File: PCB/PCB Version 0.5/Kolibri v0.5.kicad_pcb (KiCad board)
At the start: 8 copper layers, 38 x 38 mm, 212 parts, among them IC1 SX1280IMLTRT, IC2 RFX2401C, IC3 SX1280IMLTRT, IC4 RFX2401C, IC5 LMR38025SDRRR, IC6 LMR38025SDRRR, J1 USB_C_Receptacle_USB2.0_16P, J2 Conn_01x04_MountingPin, J3 Conn_Coaxial_Small, J4 Conn_Coaxial_Small, J5 Conn_01x08_MountingPin, J6 Conn_01x06_MountingPin, J7 Conn_01x06_MountingPin, J8 Conn_01x03_MountingPin, J9 Micro_SD_Card_Det1, Q1 BSS138, U1 RP2350A, U10 W25Q16JVUXIQ, U2 BMI270, U3 ESP32-U4WDH, U4 TPS2116DRL, U5 AT7456E, U6 LP5912-3.3DRV, U7 TPS746-3.3DRV, U8 WE-TVS-824015043, U9 TLV9002S_RUG_X2QFN, Y1 Crystal_GND24, Y2 Crystal_GND24, Y3 Crystal_GND24, Y4 Crystal_GND24, Y5 Crystal_GND24

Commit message: wip backup
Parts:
- removed S1: Goertek SPL06-001, Kolibri custom:Goertek SPL06-001
- added U11: LPS22HB, Package_LGA:ST_HLGA-10_2x2mm_P0.5mm_LayoutBorder3x2y, F.Cu at (124.0, 107.0)
- C25, C26, C27, C28, C29, C30, C31, C33, C34, C35, C36, C37, C38, C39, C40, C49, C50, C53, C54: footprint Capacitor_SMD:C_0402_1005Metric -> Capacitor_SMD:C_0402_1005Metric_Pad0.74x0.62mm_HandSolder
- C66, C72, D14, D15, D16, D17, D18, J7, P10, P11: moved to B.Cu
- C67, C70, C77, C78: footprint Capacitor_SMD:C_0402_1005Metric -> Capacitor_SMD:C_0402_1005Metric_Pad0.74x0.62mm_HandSolder; moved to B.Cu
- J8: moved to F.Cu
- L2: footprint Inductor_SMD:L_0402_1005Metric -> Inductor_SMD:L_0402_1005Metric_Pad0.77x0.64mm_HandSolder
- R10, R11, R12, R9: footprint Resistor_SMD:R_0402_1005Metric -> Resistor_SMD:R_0402_1005Metric_Pad0.72x0.64mm_HandSolder
- R15, R16, R19, R20, R25, R28, R29, R30, R31, R32: footprint Resistor_SMD:R_0402_1005Metric -> Resistor_SMD:R_0402_1005Metric_Pad0.72x0.64mm_HandSolder; moved to B.Cu
- moved C16 89.5 mm to (106.9, 78.8)
- moved D1 83.5 mm to (106.8, 77.2)
- moved J7 83.4 mm to (92.3, 85.0)
- moved J6 80.4 mm to (95.2, 85.0), turned to 180 degrees
- moved R5 73.3 mm to (88.8, 114.8), turned to -90 degrees
- moved C23 67.4 mm to (127.4, 105.6)
- moved C24 67.4 mm to (127.4, 107.6)
- moved R6 60.8 mm to (101.4, 116.6), turned to -90 degrees
- moved P18 58.3 mm to (114.5, 108.5)
- moved P28 57.8 mm to (117.0, 106.0)
- moved P23 55.8 mm to (114.5, 103.5)
- moved P19 54.4 mm to (114.5, 106.0)
- moved P29 48.2 mm to (118.0, 68.2)
- moved P34 48.2 mm to (115.3, 72.7)
- moved C78 39.5 mm to (110.0, 104.0), turned to 180 degrees
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
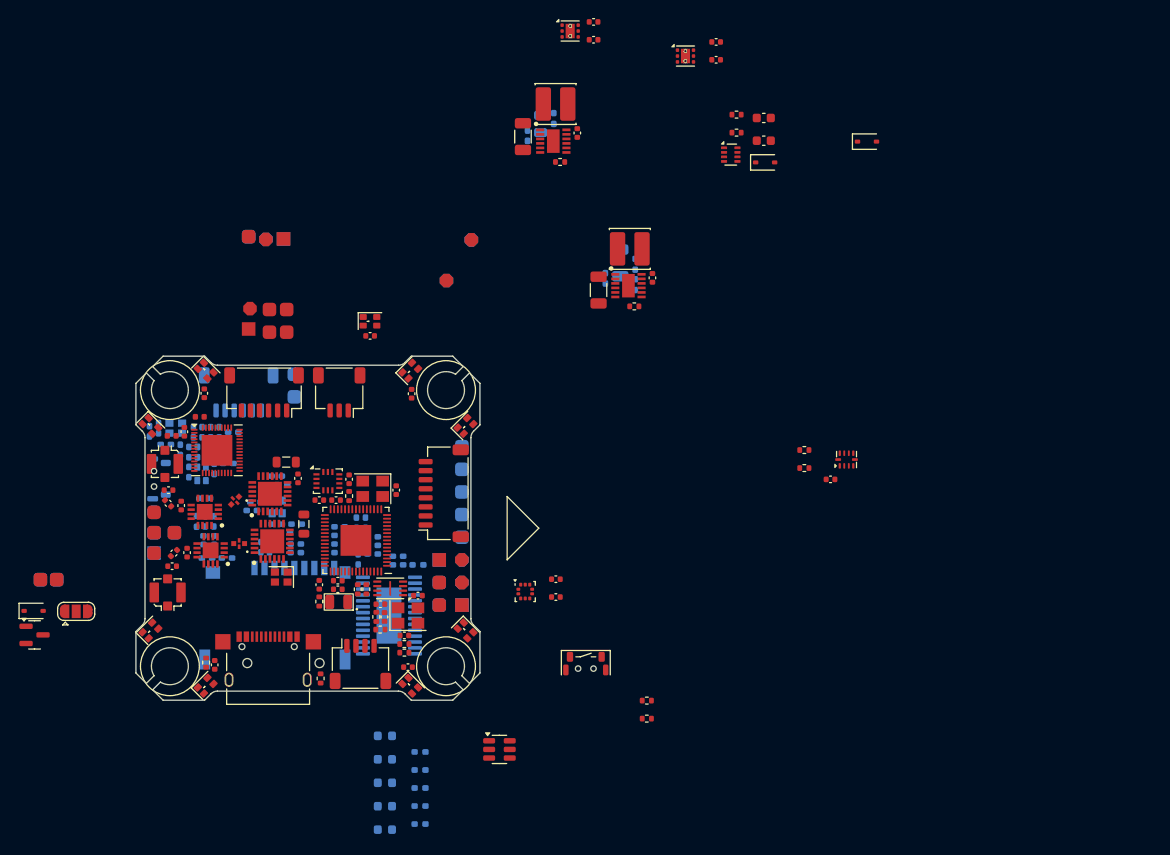
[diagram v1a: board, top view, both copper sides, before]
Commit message: preliminary layout
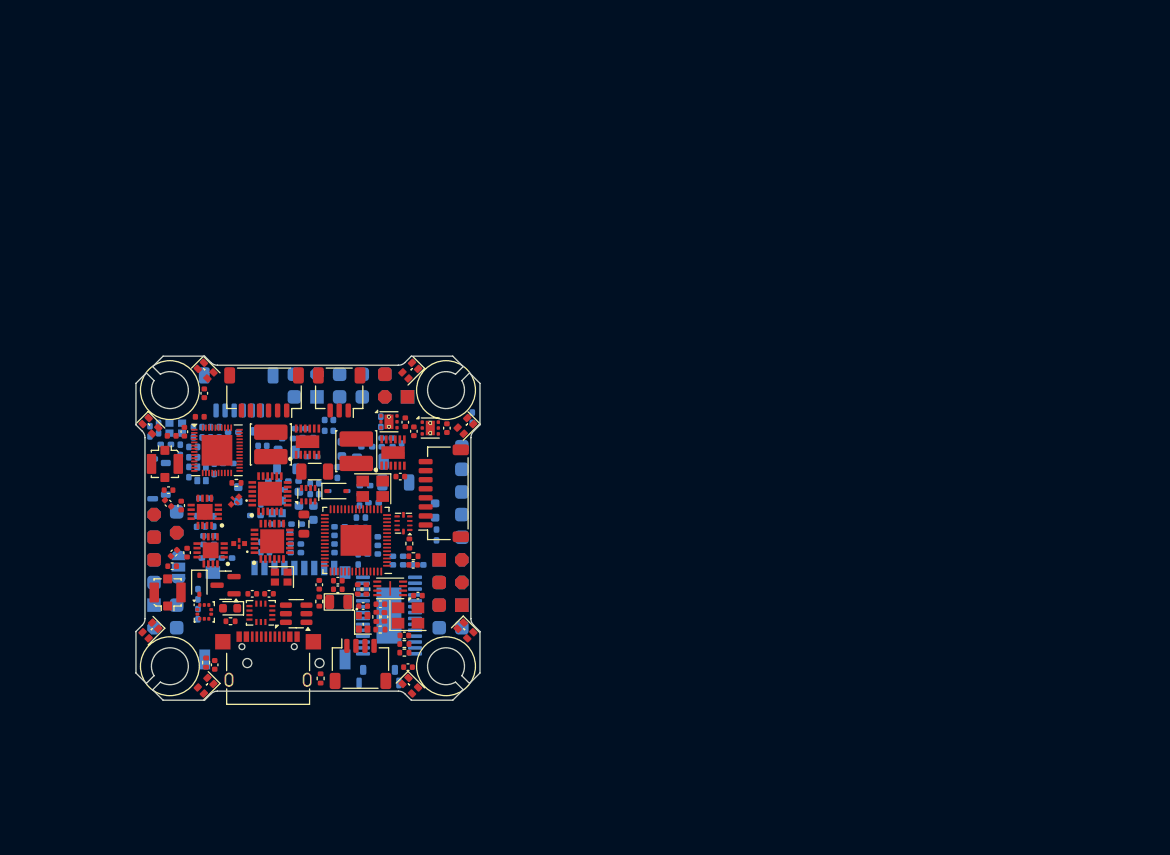
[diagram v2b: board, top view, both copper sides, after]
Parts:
- C14, C15, C17, C23, C24, C41, C65, C71, C84: footprint Capacitor_SMD:C_0402_1005Metric -> Capacitor_SMD:C_0402_1005Metric_Pad0.74x0.62mm_HandSolder; moved to B.Cu
- C63, C64, C68, D10, JP1, L5, P12, P13, P14, P15, P26, P32, P6, P7, P8, P9: moved to B.Cu
- C67: footprint Capacitor_SMD:C_0402_1005Metric_Pad0.74x0.62mm_HandSolder -> Capacitor_SMD:C_0402_1005Metric; moved to F.Cu
- D17: moved to F.Cu
- R13, R14, R17, R18, R4, R7, R8: footprint Resistor_SMD:R_0402_1005Metric -> Resistor_SMD:R_0402_1005Metric_Pad0.72x0.64mm_HandSolder; moved to B.Cu
- R31, R32: footprint Resistor_SMD:R_0402_1005Metric_Pad0.72x0.64mm_HandSolder -> Resistor_SMD:R_0402_1005Metric; moved to F.Cu
- SW1: footprint Kolibri custom:Button C530669 -> Kolibri custom:Button C530669 wo holes; moved to B.Cu
- SW2: footprint Kolibri custom:Button C530669 -> Kolibri custom:Button C530669 wo holes
- moved D10 70.0 mm to (103.3, 95.9), turned to 180 degrees
- moved C63 66.4 mm to (99.0, 96.8), turned to 90 degrees
- moved C64 64.5 mm to (100.6, 98.3), turned to 90 degrees
- moved R13 62.7 mm to (100.2, 95.7), turned to -90 degrees
- moved R14 60.6 mm to (101.2, 95.7), turned to 90 degrees
- moved U4 59.9 mm to (100.0, 96.3), turned to 90 degrees
- moved D13 59.7 mm to (103.2, 95.9)
- moved C82 52.9 mm to (111.7, 89.3), turned to -90 degrees
- moved C81 52.0 mm to (115.3, 89.0), turned to -90 degrees
- moved U6 49.8 mm to (113.5, 88.9)
- moved U9 49.4 mm to (110.5, 99.5), turned to 90 degrees
- moved L8 49.0 mm to (95.9, 90.8), turned to -90 degrees
- moved C83 48.9 mm to (110.8, 88.3), turned to -90 degrees
- moved R19 48.5 mm to (95.5, 91.5), turned to 90 degrees
- moved C84 48.3 mm to (108.0, 88.2), turned to -90 degrees
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
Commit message: moved some components
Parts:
- C54: footprint Capacitor_SMD:C_0402_1005Metric_Pad0.74x0.62mm_HandSolder -> Capacitor_SMD:C_0402_1005Metric; moved to F.Cu
- moved C40 4.93 mm to (86.8, 96.2), turned to -90 degrees
- moved R12 3.28 mm to (91.8, 100.1), turned to 0 degrees
- moved R28 2.40 mm to (111.8, 100.8)
- moved D14 2.40 mm to (111.7, 98.2)
- moved C53 1.79 mm to (90.5, 102.8), turned to 0 degrees
- moved C75 1.06 mm to (99.5, 101.0)
- moved C74 0.97 mm to (99.5, 102.2)
- moved C54 0.87 mm to (91.8, 103.7), turned to 90 degrees
- moved C6 0.85 mm to (103.5, 99.0)
- moved C17 0.78 mm to (117.6, 88.3), turned to 90 degrees
- moved D11 0.76 mm to (88.4, 94.8), turned to -90 degrees
- moved R29 0.70 mm to (93.8, 91.2)
- moved R8 0.65 mm to (103.5, 88.7)
- moved C15 0.62 mm to (107.4, 96.6)
- moved C55 0.59 mm to (94.6, 101.5)
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
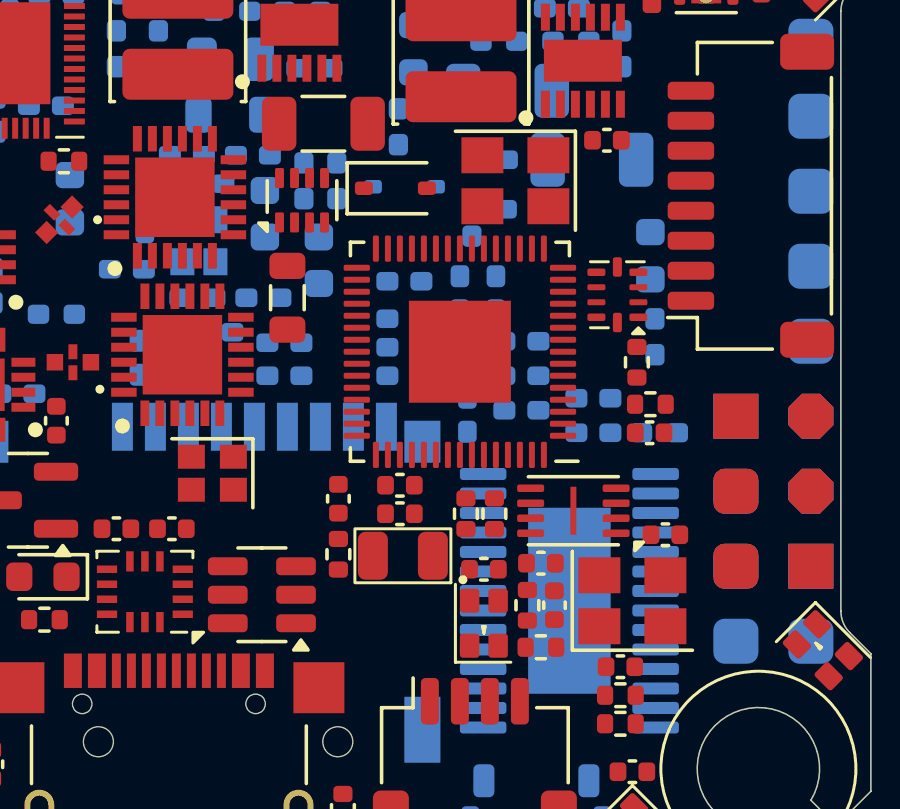
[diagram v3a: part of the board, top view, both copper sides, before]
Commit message: 3d model assignment (partially incorrect without another choice)
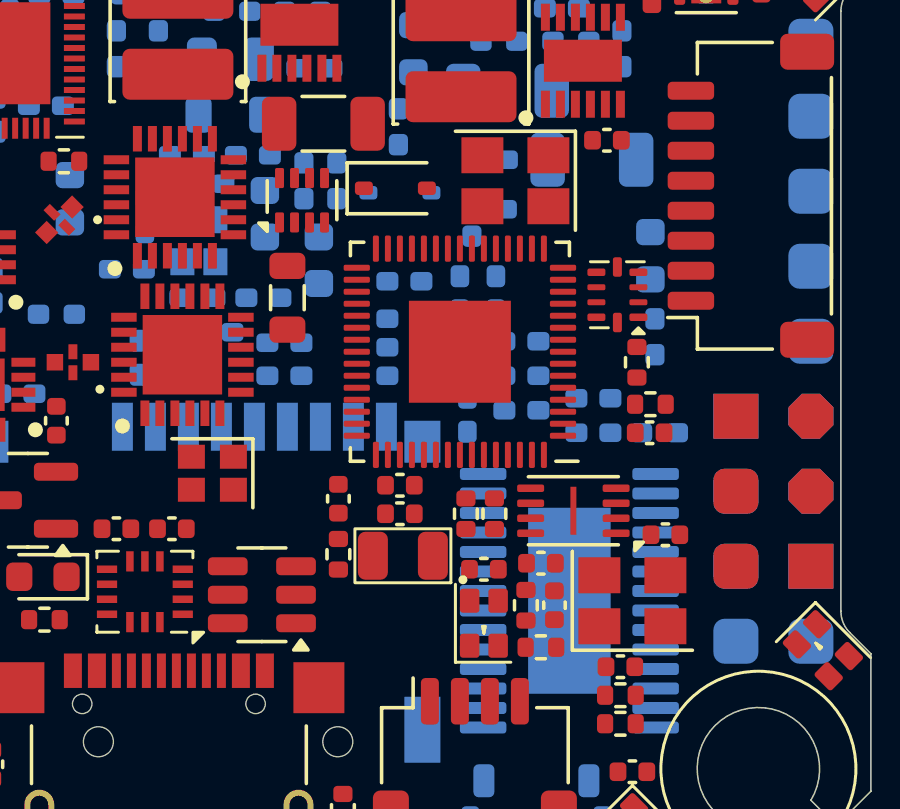
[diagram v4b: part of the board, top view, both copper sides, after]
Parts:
- moved D10 0.25 mm to (103.3, 96.0)

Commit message: wip routing
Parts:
- added C48: 100n, Capacitor_SMD:C_0402_1005Metric, F.Cu at (106.0, 110.3)
- added C56: 100n, Capacitor_SMD:C_0402_1005Metric_Pad0.74x0.62mm_HandSolder, B.Cu at (104.6, 108.4)
- added C86: 100n, Capacitor_SMD:C_0402_1005Metric_Pad0.74x0.62mm_HandSolder, B.Cu at (113.3, 108.0)
- added R33: 1k, Resistor_SMD:R_0402_1005Metric_Pad0.72x0.64mm_HandSolder, B.Cu at (111.2, 115.8)
- P14: moved to F.Cu
- moved D1 7.56 mm to (99.7, 106.3)
- moved C16 7.56 mm to (99.7, 104.5)
- moved U9 4.29 mm to (111.8, 103.5)
- moved R27 3.05 mm to (112.8, 106.0), turned to -90 degrees
- moved P14 2.50 mm to (114.5, 108.5), turned to 90 degrees
- moved P18 2.50 mm to (114.5, 111.0)
- moved C73 1.91 mm to (111.8, 106.0), turned to 90 degrees
- moved R26 0.80 mm to (111.2, 100.9)
- moved C82 0.30 mm to (111.7, 89.0)
- moved R7 0.20 mm to (102.0, 88.7)
- moved C35 0.11 mm to (85.8, 91.7)
- moved C34 0.11 mm to (86.8, 91.7)
- moved C36 0.11 mm to (86.8, 93.9)
- moved L2 0.11 mm to (87.8, 91.7)
- moved C33 0.11 mm to (89.3, 91.0)
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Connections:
- J6 pad MP: unconnected-(J6-MountPin-PadMP) -> GND
- J9 pad 8: /SD_DAT.3 -> /SD_DAT.1
- JP1 pad 1: VCC -> +10V
- JP1 pad 3: +10V -> VCC
- P6 pad 1: /U1.TX -> /U1.RX
- P7 pad 1: /U1.RX -> /U1.TX
- SW1 pad 1: Net-(U1-QSPI_SS) -> Net-(R33-Pad2)
- U1 pad 31: /RP2350/SPI0.MOSI -> /SPI0.SDX
- U1 pad 32: /Motor.1 -> /Motor.4
- U1 pad 33: /Motor.2 -> /Motor.3
- U1 pad 34: /Motor.3 -> /Motor.2
- U1 pad 35: /Motor.4 -> /Motor.1
- U5 pad 10: /SPI1.MISO -> /SPI1.SCLK
- U8 pad 4: /USB.D+ -> /USB.D-
- U8 pad 6: /USB.D- -> /USB.D+
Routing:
- net GND: track 0.00 -> 59.6 mm, vias 0 -> 125
- net +3V3: track 0.00 -> 59.4 mm, vias 0 -> 27
- net /USB.D-: track 0.00 -> 30.9 mm
- net /USB.D+: track 0.00 -> 30.2 mm, vias 0 -> 2
- net +5V: track 0.00 -> 27.6 mm, vias 0 -> 27
- net /SD_DAT.2: track 0.00 -> 23.3 mm, vias 0 -> 3
- net +5V_USB: track 0.00 -> 23.1 mm, vias 0 -> 6
- net Net-(D3-DOUT): track 0.00 -> 22.5 mm, vias 0 -> 2
- net Net-(D7-DOUT): track 0.00 -> 22.4 mm, vias 0 -> 2
- net Net-(D5-DOUT): track 0.00 -> 22.4 mm, vias 0 -> 2
- net /SD_DAT.3: track 0.00 -> 21.3 mm, vias 0 -> 3
- net /Motor.2: track 0.00 -> 21.0 mm, vias 0 -> 2
- net /Motor.1: track 0.00 -> 20.5 mm, vias 0 -> 2
- net /ELRS/WIFI_ANTENNA: track 0.00 -> 20.1 mm, vias 0 -> 1
- net /RP2350/SD_CMD: track 0.00 -> 19.7 mm, vias 0 -> 2
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- added copper zone on In6.Cu, net +10V
- added copper zone on F.Cu, net +1V1
- added copper zone on In2.Cu, net +1V1
- added copper zone on In3.Cu, net +3V3
- added copper zone on In3.Cu, net +3V3_ELRS
- added copper zone on In6.Cu, net +4V5
- added copper zone on In3.Cu, net +5V
- added copper zone on In6.Cu, net +5V
- added copper zone on B.Cu, net GND
- added copper zone on F.Cu, net GND
- added copper zone on In1.Cu, net GND
- added copper zone on In2.Cu, net GND
- added copper zone on In4.Cu, net GND
- added copper zone on In5.Cu, net GND
- added copper zone on F.Cu, net Net-(IC5-SW_1)
- added copper zone on F.Cu, net Net-(IC6-SW_1)
- added copper zone on F.Cu, net Net-(U1-VREG_LX)
- added copper zone on B.Cu, net VCC
- added copper zone on F.Cu, net VCC
- added copper zone on In6.Cu, net VCC
- added copper zone on F.Cu, net VDD3P3

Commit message: wip backup
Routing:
- net /U0.RX: track 1.99 -> 81.0 mm, vias 1 -> 3
- net /U0.TX: track 1.50 -> 74.1 mm, vias 1 -> 3
- net /I2C0.SCL: track 16.4 -> 73.6 mm, vias 2 -> 4
- net /I2C0.SDA: track 17.7 -> 74.3 mm, vias 2 -> 3
- net /SPI1.MOSI: track 2.36 -> 24.2 mm, vias 1 -> 2
- net /U1.RX: track 13.5 -> 34.8 mm, vias 2 -> 3
- net /SPI1.MISO: track 2.03 -> 22.6 mm, vias 1 -> 2
- net /U1.TX: track 11.4 -> 30.5 mm, vias 2 -> 3
- net /RP2350/OSD_SS: track 0.94 -> 18.0 mm, vias 1 -> 2
- net /Connectors/Curr_ESC: track 16.2 -> 32.1 mm, vias 1 -> 3
- net /SPI1.SCLK: track 1.48 -> 17.1 mm, vias 1 -> 2
- net /ADC/VBat_HI: track 7.01 -> 20.7 mm, vias 0 -> 3
- net +5V: track 27.6 -> 31.5 mm, vias 27 -> 28
- net +3V3: track 59.4 -> 62.8 mm, vias 27 -> 28
